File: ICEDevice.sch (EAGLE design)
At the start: 3 parts, among them IC1 TL084CNSR, U1 328P

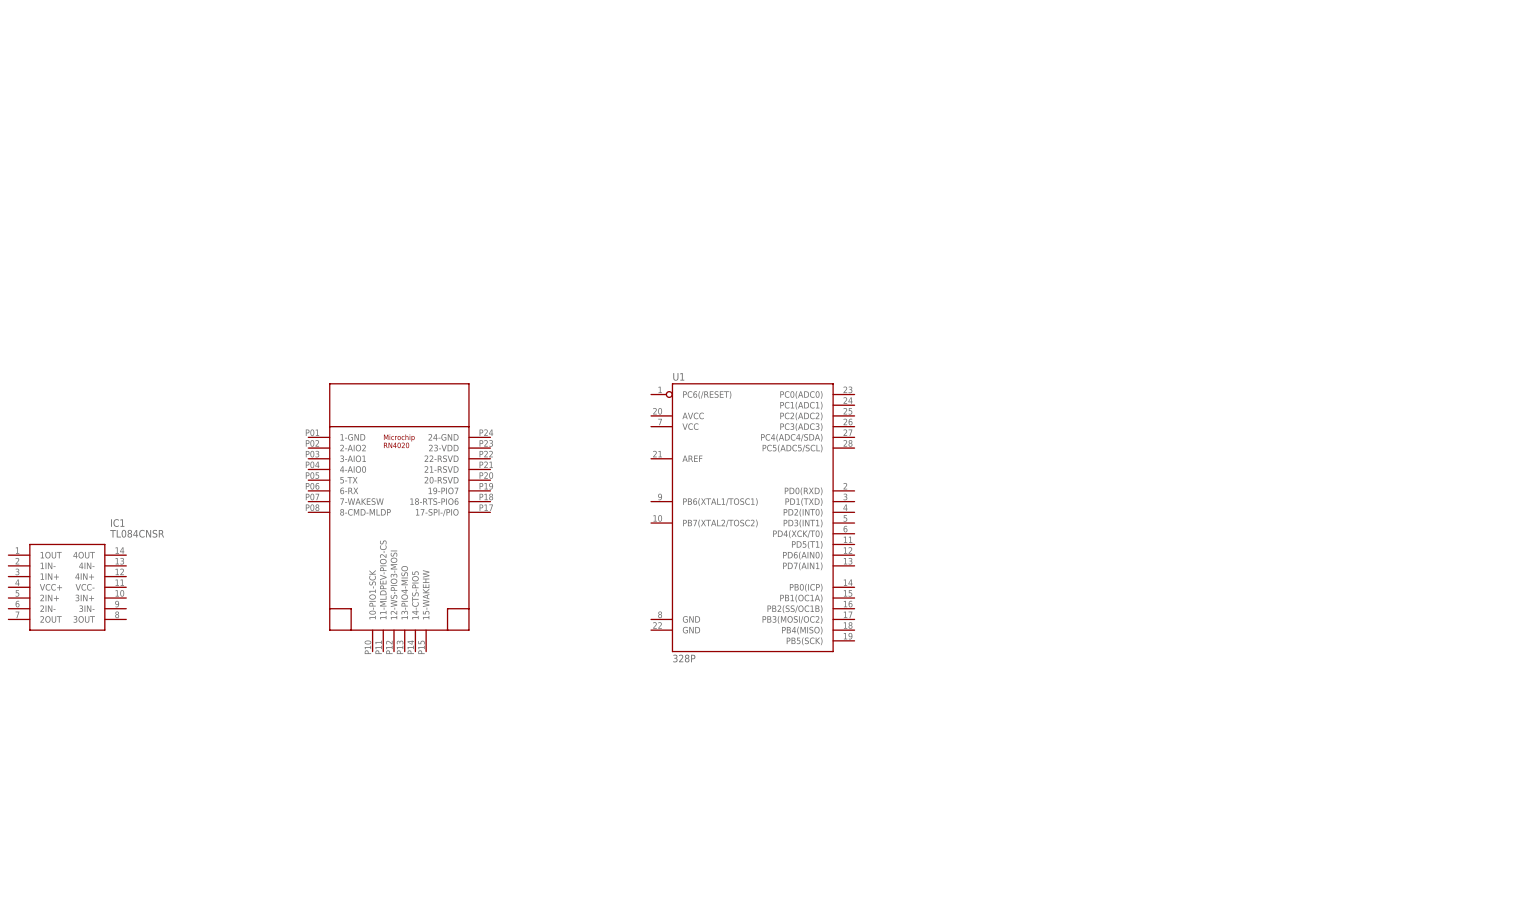
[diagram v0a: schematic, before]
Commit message: Started adding resistors for the amplification setup
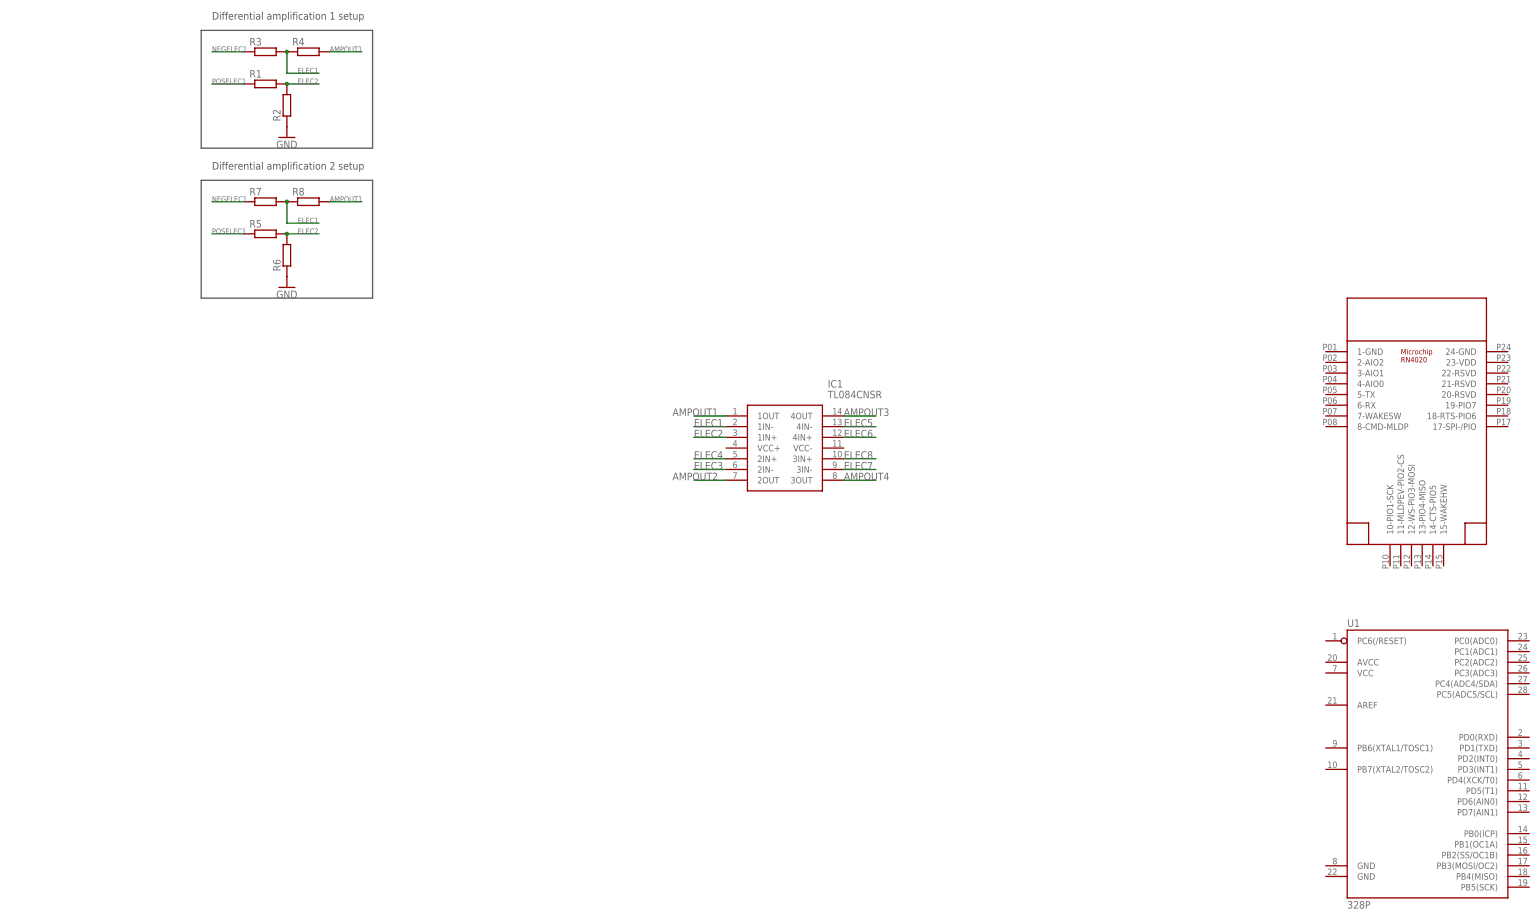
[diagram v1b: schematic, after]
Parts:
- added R1, R2, R3, R4, R5, R6, R7, R8: (no value), resistor:R-EU_0309/10
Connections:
- new net AMPOUT1: IC1.1OUT, R4.2, R8.2
- new net AMPOUT2: IC1.2OUT
- new net AMPOUT3: IC1.4OUT
- new net AMPOUT4: IC1.3OUT
- new net ELEC1: IC1.1IN-, R3.2, R4.1, R7.2, R8.1
- new net ELEC2: IC1.1IN+, R1.2, R2.2, R5.2, R6.2
- new net ELEC3: IC1.2IN-
- new net ELEC4: IC1.2IN+
- new net ELEC5: IC1.4IN-
- new net ELEC6: IC1.4IN+
- new net ELEC7: IC1.3IN-
- new net ELEC8: IC1.3IN+
- new net GND: R2.1, R6.1
- new net NEGELEC1: R3.1, R7.1
- new net POSELEC1: R1.1, R5.1
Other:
- note added: "Differential amplification 1 setup"
- note added: "Differential amplification 2 setup"
- moved on the sheet: IC1, U1
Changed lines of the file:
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@@
 <setting verticaltext="up"/>
 </settings>
-<grid distance="0.1" unitdist="inch" unit="inch" style="lines" multiple="1" display="no" altdistance="0.01" altunitdist="inch" altunit="inch"/>
+<grid distance="0.1" unitdist="inch" unit="inch" style="lines" multiple="1" display="no" altdistance="0.00393700787" altunitdist="inch" altunit="inch"/>
 <layers>
 <layer number="1" name="Top" color="4" fill="1" visible="no" active="no"/>
@@
 <part name="U1" library="SparkFun-IC-Microcontroller" library_urn="urn:adsk.eagle:library:525" deviceset="ATMEGA328P_PDIP" device="" package3d_urn="urn:adsk.eagle:package:38942/1" value="328P"/>
 <part name="IC1" library="TL084CNSR" deviceset="TL084CNSR" device=""/>
+<part name="R1" library="resistor" library_urn="urn:adsk.eagle:library:348" deviceset="R-EU_" device="0309/10" package3d_urn="urn:adsk.eagle:package:23567/1"/>
+<part name="R2" library="resistor" library_urn="urn:adsk.eagle:library:348" deviceset="R-EU_" device="0309/10" package3d_urn="urn:adsk.eagle:package:23567/1"/>
+<part name="R3" library="resistor" library_urn="urn:adsk.eagle:library:348" deviceset="R-EU_" device="0309/10" package3d_urn="urn:adsk.eagle:package:23567/1"/>
+<part name="R4" library="resistor" library_urn="urn:adsk.eagle:library:348" deviceset="R-EU_" device="0309/10" package3d_urn="urn:adsk.eagle:package:23567/1"/>
+<part name="GND2" library="supply1" library_urn="urn:adsk.eagle:library:371" deviceset="GND" device=""/>
+<part name="FRAME1" library="frames" library_urn="urn:adsk.eagle:library:229" deviceset="A4L-LOC" device=""/>
+<part name="R5" library="resistor" library_urn="urn:adsk.eagle:library:348" deviceset="R-EU_" device="0309/10" package3d_urn="urn:adsk.eagle:package:23567/1"/>
+<part name="R6" library="resistor" library_urn="urn:adsk.eagle:library:348" deviceset="R-EU_" device="0309/10" package3d_urn="urn:adsk.eagle:package:23567/1"/>
+<part name="R7" library="resistor" library_urn="urn:adsk.eagle:library:348" deviceset="R-EU_" device="0309/10" package3d_urn="urn:adsk.eagle:package:23567/1"/>
+<part name="R8" library="resistor" library_urn="urn:adsk.eagle:library:348" deviceset="R-EU_" device="0309/10" package3d_urn="urn:adsk.eagle:package:23567/1"/>
+<part name="GND1" library="supply1" library_urn="urn:adsk.eagle:library:371" deviceset="GND" device=""/>
 </parts>
 <sheets>
 <sheet>
 <plain>
+<wire x1="7.62" y1="167.64" x2="7.62" y2="139.7" width="0.1524" layer="97"/>
+<wire x1="7.62" y1="139.7" x2="48.26" y2="139.7" width="0.1524" layer="97"/>
+<wire x1="48.26" y1="139.7" x2="48.26" y2="167.64" width="0.1524" layer="97"/>
+<wire x1="48.26" y1="167.64" x2="7.62" y2="167.64" width="0.1524" layer="97"/>
+<text x="10.16" y="170.18" size="1.778" layer="97">Differential amplification 1 setup</text>
+<wire x1="7.62" y1="132.08" x2="7.62" y2="104.14" width="0.1524" layer="97"/>
+<wire x1="7.62" y1="104.14" x2="48.26" y2="104.14" width="0.1524" layer="97"/>
+<wire x1="48.26" y1="104.14" x2="48.26" y2="132.08" width="0.1524" layer="97"/>
+<wire x1="48.26" y1="132.08" x2="7.62" y2="132.08" width="0.1524" layer="97"/>
+<text x="10.16" y="134.62" size="1.778" layer="97">Differential amplification 2 setup</text>
 </plain>
 <instances>
-<instance part="U$1" gate="G$1" x="55.88" y="50.8"/>
-<instance part="U1" gate="G$1" x="137.16" y="55.88"/>
-<instance part="IC1" gate="G$1" x="-38.1" y="43.18"/>
+<instance part="U$1" gate="G$1" x="297.18" y="71.12"/>
+<instance part="U1" gate="G$1" x="297.18" y="-2.54"/>
+<instance part="IC1" gate="G$1" x="132.08" y="76.2"/>
+<instance part="R1" gate="G$1" x="22.86" y="154.94"/>
+<instance part="R2" gate="G$1" x="27.94" y="149.86" rot="R90"/>
+<instance part="R3" gate="G$1" x="22.86" y="162.56"/>
+<instance part="R4" gate="G$1" x="33.02" y="162.56"/>
+<instance part="GND2" gate="1" x="27.94" y="142.24"/>
+<instance part="FRAME1" gate="G$1" x="0" y="0"/>
+<instance part="R5" gate="G$1" x="22.86" y="119.38"/>
+<instance part="R6" gate="G$1" x="27.94" y="114.3" rot="R90"/>
+<instance part="R7" gate="G$1" x="22.86" y="127"/>
+<instance part="R8" gate="G$1" x="33.02" y="127"/>
+<instance part="GND1" gate="1" x="27.94" y="106.68"/>
 </instances>
 <busses>
 </busses>
 <nets>
+<net name="GND" class="0">
+<segment>
+<pinref part="R2" gate="G$1" pin="1"/>
+<pinref part="GND2" gate="1" pin="GND"/>
+</segment>
+<segment>
+<pinref part="R6" gate="G$1" pin="1"/>
+<pinref part="GND1" gate="1" pin="GND"/>
+</segment>
+</net>
+<net name="ELEC1" class="0">
+<segment>
+<pinref part="IC1" gate="G$1" pin="1IN-"/>
+<wire x1="132.08" y1="73.66" x2="124.46" y2="73.66" width="0.1524" layer="91"/>
+<label x="124.46" y="73.66" size="1.778" layer="95"/>
+</segment>
+<segment>
+<pinref part="R3" gate="G$1" pin="2"/>
+<pinref part="R4" gate="G$1" pin="1"/>
+<wire x1="27.94" y1="162.56" x2="27.94" y2="157.48" width="0.1524" layer="91"/>
+<wire x1="27.94" y1="157.48" x2="35.56" y2="157.48" width="0.1524" layer="91"/>
+<junction x="27.94" y="162.56"/>
+<label x="30.48" y="157.48" size="1.27" layer="95"/>
+</segment>
+<segment>
+<pinref part="R7" gate="G$1" pin="2"/>
+<pinref part="R8" gate="G$1" pin="1"/>
+<wire x1="27.94" y1="127" x2="27.94" y2="121.92" width="0.1524" layer="91"/>
+<wire x1="27.94" y1="121.92" x2="35.56" y2="121.92" width="0.1524" layer="91"/>
+<junction x="27.94" y="127"/>
+<label x="30.48" y="121.92" size="1.27" layer="95"/>
+</segment>
+</net>
+<net name="ELEC2" class="0">
+<segment>
+<pinref part="IC1" gate="G$1" pin="1IN+"/>
+<wire x1="132.08" y1="71.12" x2="124.46" y2="71.12" width="0.1524" layer="91"/>
+<label x="124.46" y="71.12" size="1.778" layer="95"/>
+</segment>
+<segment>
+<pinref part="R1" gate="G$1" pin="2"/>
+<pinref part="R2" gate="G$1" pin="2"/>
+<wire x1="27.94" y1="154.94" x2="35.56" y2="154.94" width="0.1524" layer="91"/>
+<junction x="27.94" y="154.94"/>
+<label x="30.48" y="154.94" size="1.27" layer="95"/>
+</segment>
+<segment>
+<pinref part="R5" gate="G$1" pin="2"/>
+<pinref part="R6" gate="G$1" pin="2"/>
+<wire x1="27.94" y1="119.38" x2="35.56" y2="119.38" width="0.1524" layer="91"/>
+<junction x="27.94" y="119.38"/>
+<label x="30.48" y="119.38" size="1.27" layer="95"/>
+</segment>
+</net>
+<net name="ELEC4" class="0">
+<segment>
+<pinref part="IC1" gate="G$1" pin="2IN+"/>
+<wire x1="132.08" y1="66.04" x2="124.46" y2="66.04" width="0.1524" layer="91"/>
+<label x="124.46" y="66.04" size="1.778" layer="95"/>
+</segment>
+</net>
+<net name="ELEC3" class="0">
+<segment>
+<pinref part="IC1" gate="G$1" pin="2IN-"/>
+<wire x1="132.08" y1="63.5" x2="124.46" y2="63.5" width="0.1524" layer="91"/>
+<label x="124.46" y="63.5" size="1.778" layer="95"/>
+</segment>
+</net>
+<net name="ELEC7" class="0">
+<segment>
+<pinref part="IC1" gate="G$1" pin="3IN-"/>
+<wire x1="160.02" y1="63.5" x2="167.64" y2="63.5" width="0.1524" layer="91"/>
+<label x="160.02" y="63.5" size="1.778" layer="95"/>
+</segment>
+</net>
+<net name="ELEC8" class="0">
+<segment>
+<pinref part="IC1" gate="G$1" pin="3IN+"/>
+<wire x1="160.02" y1="66.04" x2="167.64" y2="66.04" width="0.1524" layer="91"/>
+<label x="160.02" y="66.04" size="1.778" layer="95"/>
+</segment>
+</net>
+<net name="ELEC6" class="0">
+<segment>
+<pinref part="IC1" gate="G$1" pin="4IN+"/>
+<wire x1="160.02" y1="71.12" x2="167.64" y2="71.12" width="0.1524" layer="91"/>
+<label x="160.02" y="71.12" size="1.778" layer="95"/>
+</segment>
+</net>
+<net name="ELEC5" class="0">
+<segment>
+<pinref part="IC1" gate="G$1" pin="4IN-"/>
+<wire x1="160.02" y1="73.66" x2="167.64" y2="73.66" width="0.1524" layer="91"/>
+<label x="160.02" y="73.66" size="1.778" layer="95"/>
+</segment>
+</net>
+<net name="POSELEC1" class="0">
+<segment>
+<pinref part="R1" gate="G$1" pin="1"/>
+<label x="10.16" y="154.94" size="1.27" layer="95"/>
+<wire x1="17.78" y1="154.94" x2="10.16" y2="154.94" width="0.1524" layer="91"/>
+</segment>
+<segment>
+<pinref part="R5" gate="G$1" pin="1"/>
+<label x="10.16" y="119.38" size="1.27" layer="95"/>
+<wire x1="17.78" y1="119.38" x2="10.16" y2="119.38" width="0.1524" layer="91"/>
+</segment>
+</net>
+<net name="NEGELEC1" class="0">
+<segment>
+<pinref part="R3" gate="G$1" pin="1"/>
+<wire x1="17.78" y1="162.56" x2="10.16" y2="162.56" width="0.1524" layer="91"/>
+<label x="10.16" y="162.56" size="1.27" layer="95"/>
+</segment>
+<segment>
+<pinref part="R7" gate="G$1" pin="1"/>
+<wire x1="17.78" y1="127" x2="10.16" y2="127" width="0.1524" layer="91"/>
+<label x="10.16" y="127" size="1.27" layer="95"/>
+</segment>
+</net>
+<net name="AMPOUT1" class="0">
+<segment>
+<pinref part="IC1" gate="G$1" pin="1OUT"/>
+<wire x1="132.08" y1="76.2" x2="124.46" y2="76.2" width="0.1524" layer="91"/>
+<label x="119.38" y="76.2" size="1.778" layer="95"/>
+</segment>
+<segment>
+<pinref part="R4" gate="G$1" pin="2"/>
+<wire x1="38.1" y1="162.56" x2="45.72" y2="162.56" width="0.1524" layer="91"/>
+<label x="38.1" y="162.56" size="1.27" layer="95"/>
+</segment>
+<segment>
+<pinref part="R8" gate="G$1" pin="2"/>
+<wire x1="38.1" y1="127" x2="45.72" y2="127" width="0.1524" layer="91"/>
+<label x="38.1" y="127" size="1.27" layer="95"/>
+</segment>
+</net>
+<net name="AMPOUT2" class="0">
+<segment>
+<pinref part="IC1" gate="G$1" pin="2OUT"/>
+<wire x1="132.08" y1="60.96" x2="124.46" y2="60.96" width="0.1524" layer="91"/>
+<label x="119.38" y="60.96" size="1.778" layer="95"/>
+</segment>
+</net>
+<net name="AMPOUT3" class="0">
+<segment>
+<pinref part="IC1" gate="G$1" pin="4OUT"/>
+<wire x1="160.02" y1="76.2" x2="167.64" y2="76.2" width="0.1524" layer="91"/>
+<label x="160.02" y="76.2" size="1.778" layer="95"/>
+</segment>
+</net>
+<net name="AMPOUT4" class="0">
+<segment>
+<pinref part="IC1" gate="G$1" pin="3OUT"/>
+<wire x1="160.02" y1="60.96" x2="167.64" y2="60.96" width="0.1524" layer="91"/>
+<label x="160.02" y="60.96" size="1.778" layer="95"/>
+</segment>
+</net>
 </nets>
 </sheet>
